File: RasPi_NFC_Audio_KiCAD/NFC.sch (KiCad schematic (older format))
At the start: 33 parts, among them U2 PN532, Y1 Oscillator

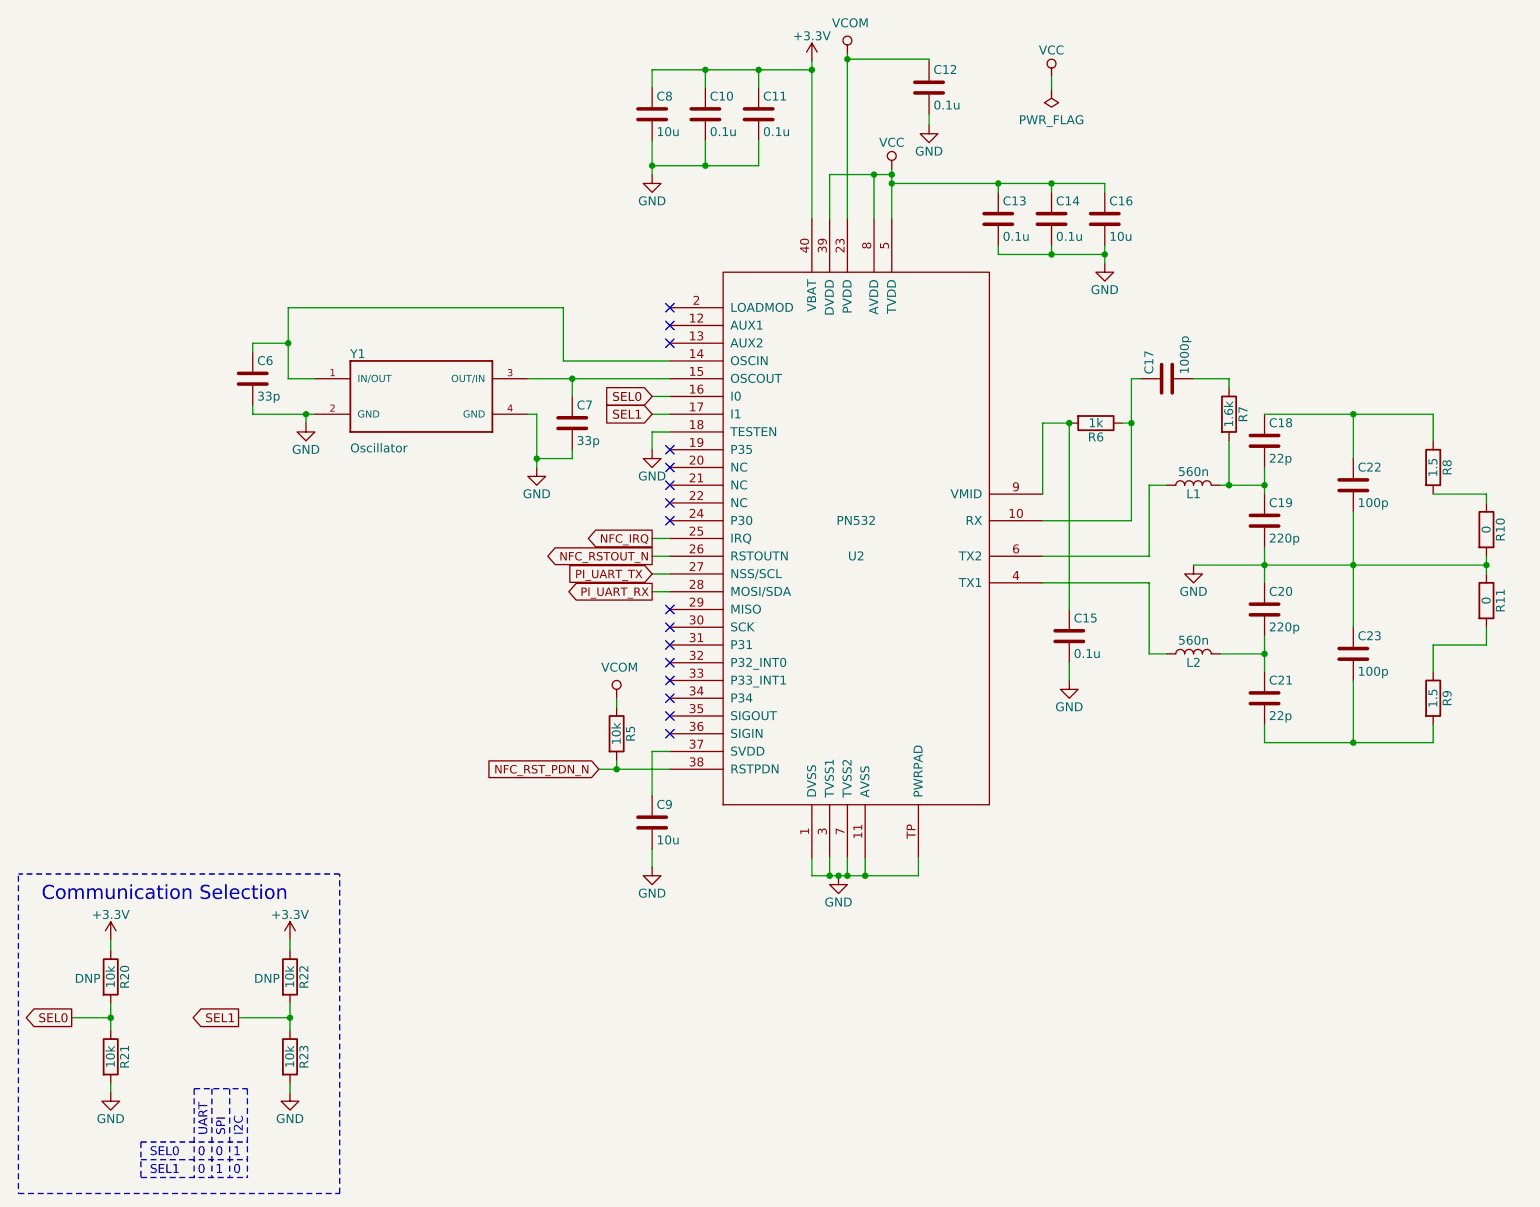
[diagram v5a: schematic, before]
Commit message: Added GPIO expander to schematic
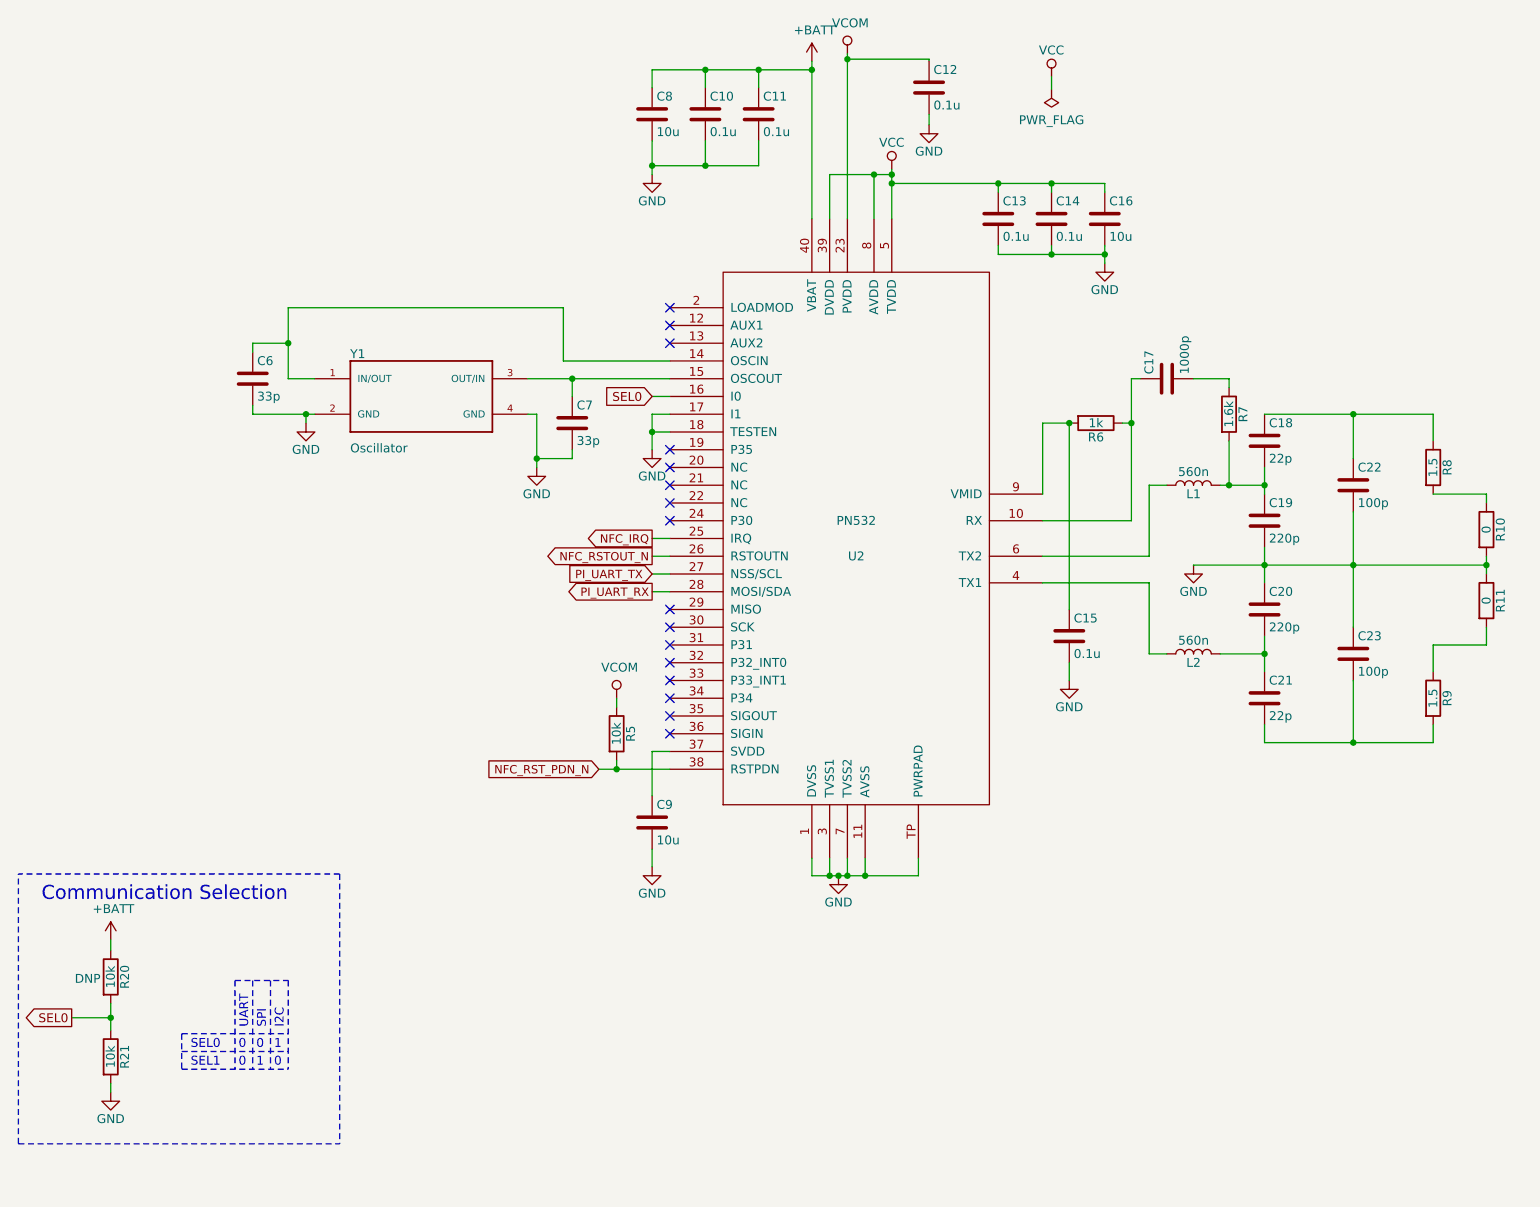
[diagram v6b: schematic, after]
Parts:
- removed R22, R23: 10k, Resistor_SMD:R_0603_1608Metric_Pad1.05x0.95mm_HandSolder, symbol Device:R
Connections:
- net SEL1 is gone; now on net GND: U2.17 (I1)
- net +3V3 renamed +BATT
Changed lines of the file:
@@
-$EndComp
-$Comp
-L power:+3.3V #PWR0116
-U 1 1 5ACE3D82
-P 6150 1050
-F 0 "#PWR0116" H 6150 900 50  0001 C CNN
-F 1 "+3.3V" H 6150 1190 50  0000 C CNN
-F 2 "" H 6150 1050 50  0001 C CNN
-F 3 "" H 6150 1050 50  0001 C CNN
-	1    6150 1050
-	1    0    0    -1
 $EndComp
 $Comp
@@
 Wire Wire Line
 	5250 3140 5350 3140
-Wire Wire Line
-	5350 3040 5250 3040
 Wire Wire Line
 	5350 2940 5250 2940
@@
 Text GLabel 5250 2940 0    50   Input ~ 0
 SEL0
-Text GLabel 5250 3040 0    50   Input ~ 0
-SEL1
 Text GLabel 1980 6440 0    50   Output ~ 0
 SEL0
@@
 	1    0    0    -1
 $EndComp
-$Comp
-L power:+3.3V #PWR0128
-U 1 1 5E1B7781
-P 2200 6000
-F 0 "#PWR0128" H 2200 5850 50  0001 C CNN
-F 1 "+3.3V" H 2200 6140 50  0000 C CNN
-F 2 "" H 2200 6000 50  0001 C CNN
-F 3 "" H 2200 6000 50  0001 C CNN
-	1    2200 6000
-	1    0    0    -1
-$EndComp
-Text GLabel 2920 6440 0    50   Output ~ 0
+Wire Notes Line
+	2600 6530 2600 6730
+Wire Notes Line
+	2600 6530 3200 6530
+Wire Notes Line
+	2600 6630 3200 6630
+Wire Notes Line
+	2600 6730 3200 6730
+Wire Notes Line
+	2900 6230 3200 6230
+Wire Notes Line
+	2900 6230 2900 6730
+Wire Notes Line
+	3200 6230 3200 6730
+Wire Notes Line
+	3100 6230 3100 6730
+Wire Notes Line
+	3000 6230 3000 6730
+Text Notes 2650 6620 0    50   ~ 0
+SEL0
+Text Notes 2650 6720 0    50   ~ 0
 SEL1
-Wire Notes Line
-	2370 7140 2370 7340
-Wire Notes Line
-	2370 7140 2970 7140
-Wire Notes Line
-	2370 7240 2970 7240
-Wire Notes Line
-	2370 7340 2970 7340
-Wire Notes Line
-	2670 6840 2970 6840
-Wire Notes Line
-	2670 6840 2670 7340
-Wire Notes Line
-	2970 6840 2970 7340
-Wire Notes Line
-	2870 6840 2870 7340
-Wire Notes Line
-	2770 6840 2770 7340
-Text Notes 2420 7230 0    50   ~ 0
-SEL0
-Text Notes 2420 7330 0    50   ~ 0
-SEL1
-Text Notes 2690 7330 0    50   ~ 0
+Text Notes 2920 6720 0    50   ~ 0
 0
-Text Notes 2690 7230 0    50   ~ 0
+Text Notes 2920 6620 0    50   ~ 0
 0
-Text Notes 2790 7230 0    50   ~ 0
+Text Notes 3020 6620 0    50   ~ 0
 0
-Text Notes 2890 7330 0    50   ~ 0
+Text Notes 3120 6720 0    50   ~ 0
 0
-Text Notes 2790 7330 0    50   ~ 0
+Text Notes 3020 6720 0    50   ~ 0
 1
-Text Notes 2890 7230 0    50   ~ 0
+Text Notes 3120 6620 0    50   ~ 0
 1
-Text Notes 2750 7110 1    50   ~ 0
+Text Notes 2980 6500 1    50   ~ 0
 UART
-Text Notes 2850 7110 1    50   ~ 0
+Text Notes 3080 6500 1    50   ~ 0
 SPI
-Text Notes 2950 7110 1    50   ~ 0
+Text Notes 3180 6500 1    50   ~ 0
 I2C
 Wire Notes Line
-	1680 5640 1680 7430
-Wire Notes Line
-	1680 7430 3490 7430
-Wire Notes Line
-	3490 7430 3490 5630
+	1680 7150 3490 7150
 Wire Notes Line
 	3490 5630 1680 5630
@@
 Wire Wire Line
 	2200 6440 2200 6510
-$Comp
-L power:GND #PWR05
-U 1 1 5E1FB945
-P 3210 6860
-F 0 "#PWR05" H 3210 6610 50  0001 C CNN
-F 1 "GND" H 3210 6710 50  0000 C CNN
-F 2 "" H 3210 6860 50  0001 C CNN
-F 3 "" H 3210 6860 50  0001 C CNN
-	1    3210 6860
-	1    0    0    -1
-$EndComp
-$Comp
-L power:+3.3V #PWR04
-U 1 1 5E1FB94B
-P 3210 6000
-F 0 "#PWR04" H 3210 5850 50  0001 C CNN
-F 1 "+3.3V" H 3210 6140 50  0000 C CNN
-F 2 "" H 3210 6000 50  0001 C CNN
-F 3 "" H 3210 6000 50  0001 C CNN
-	1    3210 6000
-	1    0    0    -1
-$EndComp
-$Comp
-L Device:R R23
-U 1 1 5E1FB953
-P 3210 6660
-F 0 "R23" V 3290 6660 50  0000 C CNN
-F 1 "10k" V 3210 6660 50  0000 C CNN
-F 2 "Resistor_SMD:R_0603_1608Metric_Pad1.05x0.95mm_HandSolder" V 3140 6660 50  0001 C CNN
-F 3 "" H 3210 6660 50  0001 C CNN
-F 4 "RNCP0603FTD10K0" H 3210 6660 50  0001 C CNN "Part #"
-F 5 "RNCP0603FTD10K0CT-ND" H 3210 6660 50  0001 C CNN "DigiKey"
-	1    3210 6660
-	1    0    0    -1
-$EndComp
-$Comp
-L Device:R R22
-U 1 1 5E1FB95C
-P 3210 6210
-F 0 "R22" V 3290 6210 50  0000 C CNN
-F 1 "10k" V 3210 6210 50  0000 C CNN
-F 2 "Resistor_SMD:R_0603_1608Metric_Pad1.05x0.95mm_HandSolder" V 3140 6210 50  0001 C CNN
-F 3 "" H 3210 6210 50  0001 C CNN
-F 4 "RNCP0603FTD10K0" H 3210 6210 50  0001 C CNN "Part #"
-F 5 "RNCP0603FTD10K0CT-ND" H 3210 6210 50  0001 C CNN "DigiKey"
-F 6 "DNP" H 3080 6200 50  0000 C CNN "DNP"
-	1    3210 6210
-	1    0    0    -1
-$EndComp
-Wire Wire Line
-	3210 6000 3210 6060
-Wire Wire Line
-	3210 6360 3210 6440
-Connection ~ 3210 6440
-Wire Wire Line
-	3210 6440 3210 6510
-Wire Wire Line
-	2920 6440 3210 6440
 Wire Wire Line
 	2200 6810 2200 6860
-Wire Wire Line
-	3210 6810 3210 6860
 $Comp
 L power:GND #PWR0132
@@
 Wire Wire Line
 	7500 1140 7500 1210
+$Comp
+L power:+BATT #PWR?
+U 1 1 5E27C64E
+P 6150 1050
+AR Path="/5E27C64E" Ref="#PWR?"  Part="1"
+AR Path="/5E17696B/5E27C64E" Ref="#PWR019"  Part="1"
+F 0 "#PWR019" H 6150 900 50  0001 C CNN
+F 1 "+BATT" H 6165 1223 50  0000 C CNN
+F 2 "" H 6150 1050 50  0001 C CNN
+F 3 "" H 6150 1050 50  0001 C CNN
+	1    6150 1050
+	1    0    0    -1
+$EndComp
+$Comp
+L power:+BATT #PWR?
+U 1 1 5E282E16
+P 2200 6000
+AR Path="/5E282E16" Ref="#PWR?"  Part="1"
+AR Path="/5E17696B/5E282E16" Ref="#PWR018"  Part="1"
+F 0 "#PWR018" H 2200 5850 50  0001 C CNN
+F 1 "+BATT" H 2215 6173 50  0000 C CNN
+F 2 "" H 2200 6000 50  0001 C CNN
+F 3 "" H 2200 6000 50  0001 C CNN
+	1    2200 6000
+	1    0    0    -1
+$EndComp
+Wire Wire Line
+	5350 3040 5250 3040
+Wire Wire Line
+	5250 3040 5250 3140
+Connection ~ 5250 3140
+Wire Notes Line
+	3490 5630 3490 7150
+Wire Notes Line
+	1680 7150 1680 5630
 $EndSCHEMATC
